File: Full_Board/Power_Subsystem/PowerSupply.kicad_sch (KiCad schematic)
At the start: 26 parts, among them IC4 LM2576HVS-5.0_NOPB, J8 KLDHCX-8-0202-A, U1 LM2576SX-3.3-NOPB

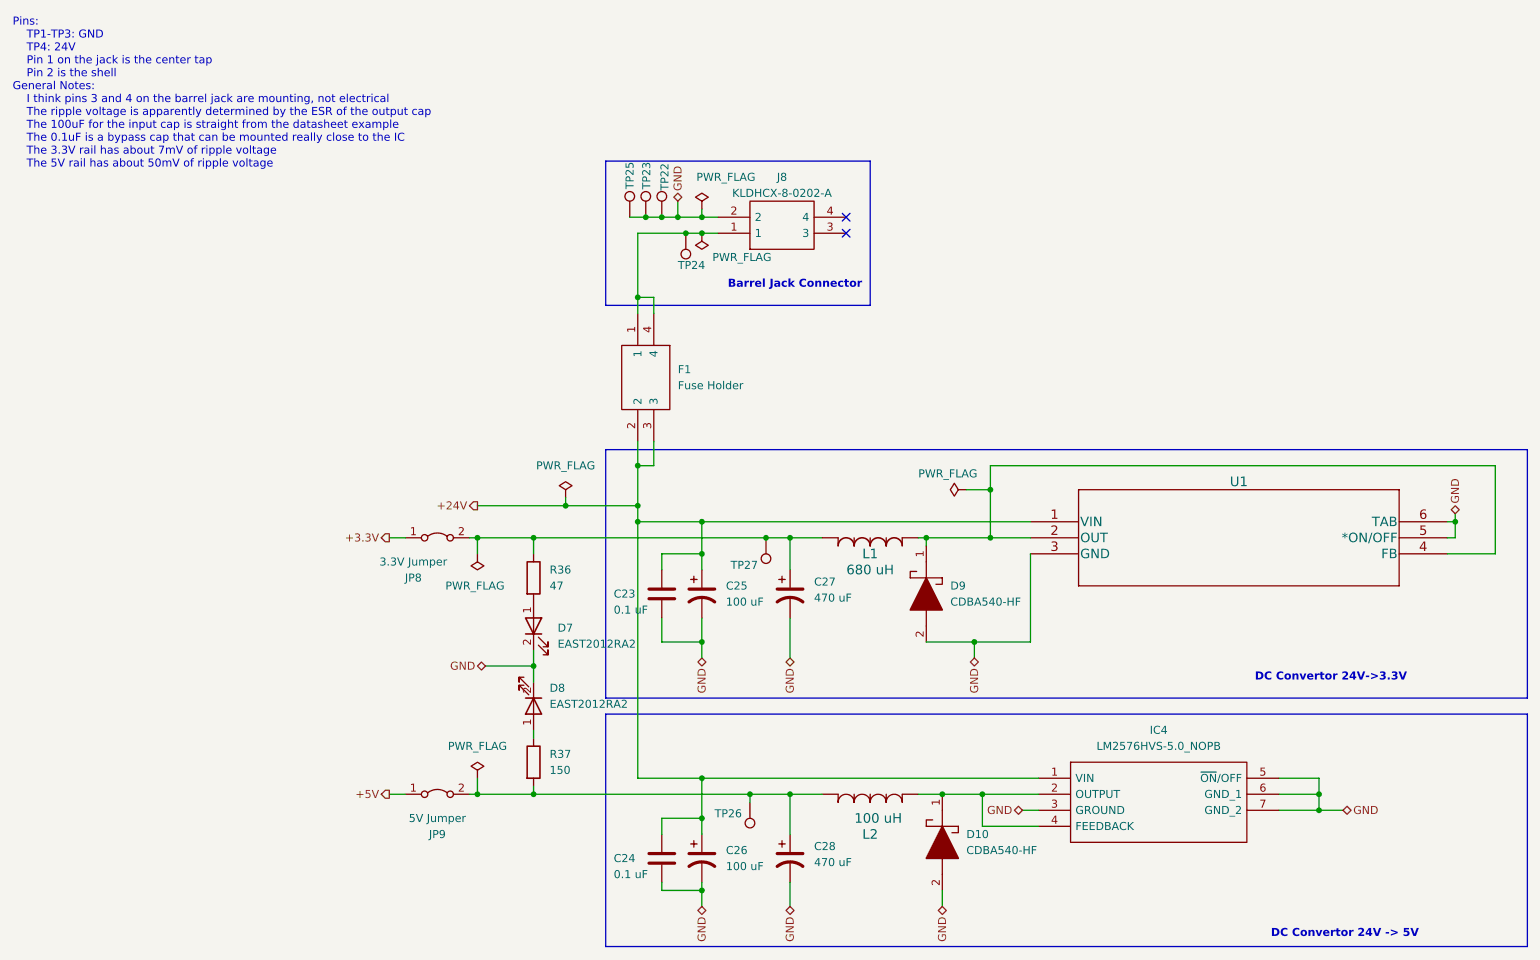
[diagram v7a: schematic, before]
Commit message: Redo pinout, finish pcb layout (no traces)
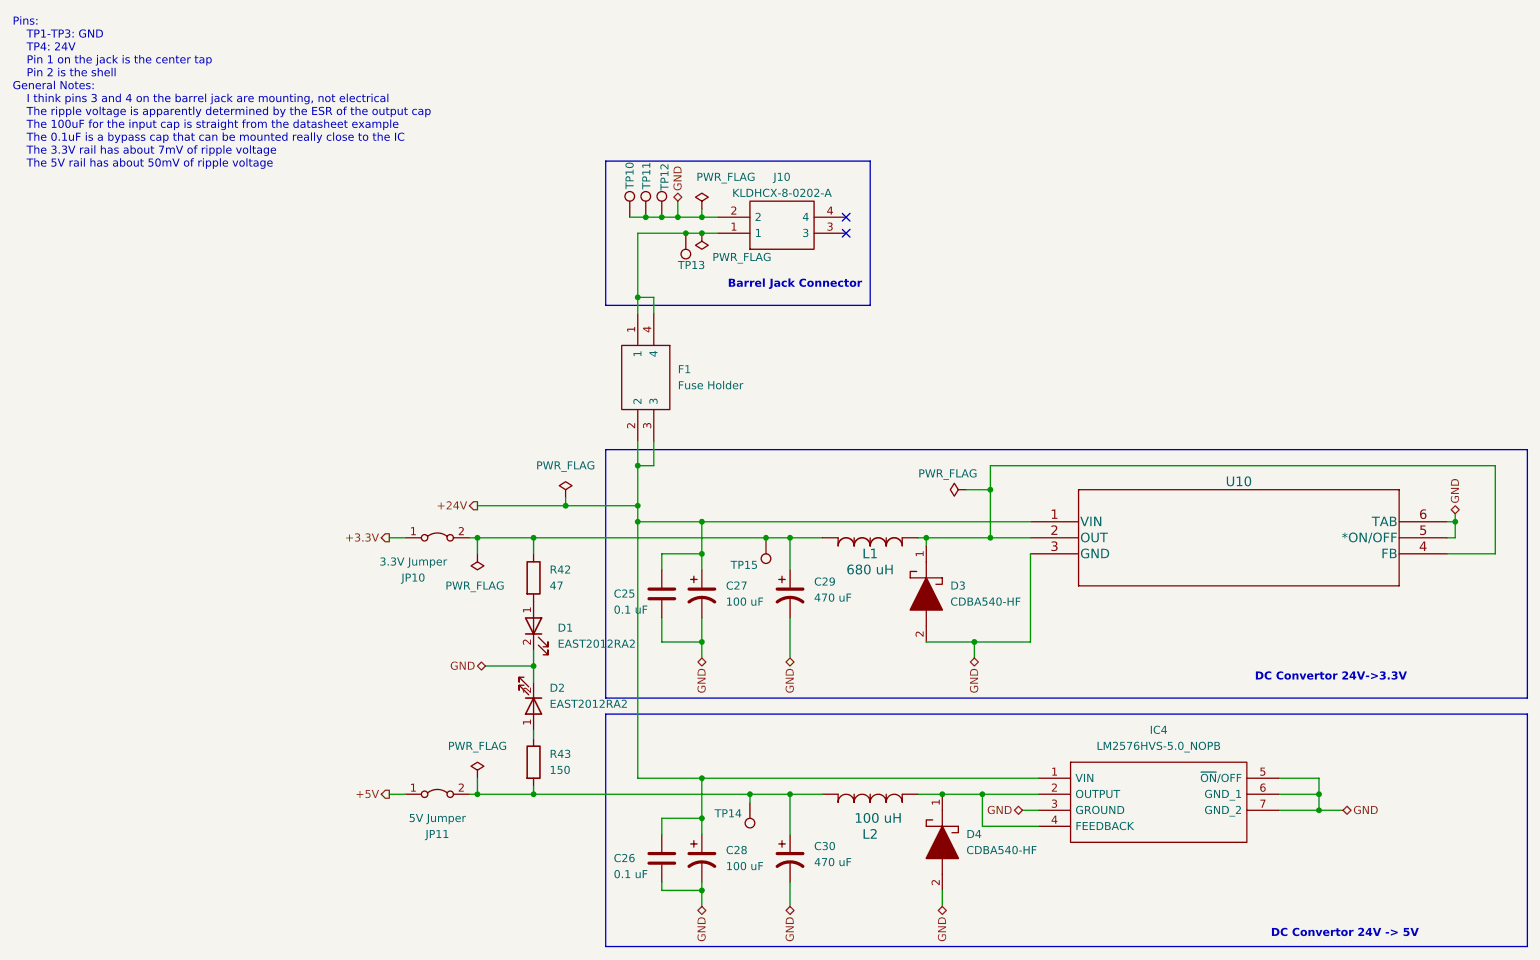
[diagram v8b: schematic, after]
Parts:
- renumbered C23 to C25, C24 to C26, C25 to C27, C26 to C28, C27 to C29, C28 to C30, D7 to D1, D8 to D2, D9 to D3, D10 to D4, J8 to J10, JP8 to JP10, JP9 to JP11, R36 to R42, R37 to R43, TP25 to TP10, TP23 to TP11, TP22 to TP12, TP24 to TP13, TP26 to TP14, TP27 to TP15, U1 to U10
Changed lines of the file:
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@@
   (symbol (lib_id "Device:C_Polarized_US") (at 140.97 146.05 0) (unit 1)
     (in_bom yes) (on_board yes) (fields_autoplaced)
-    (property "Reference" "C28" (id 0) (at 144.78 144.1449 0)
+    (property "Reference" "C30" (id 0) (at 144.78 144.1449 0)
       (effects (font (size 1.27 1.27)) (justify left))
     )
@@
   (symbol (lib_id "Device:C") (at 120.65 146.05 0) (unit 1)
     (in_bom yes) (on_board yes)
-    (property "Reference" "C24" (id 0) (at 113.03 146.05 0)
+    (property "Reference" "C26" (id 0) (at 113.03 146.05 0)
       (effects (font (size 1.27 1.27)) (justify left))
     )
@@
   (symbol (lib_id "power:PWR_FLAG") (at 127 46.99 180) (unit 1)
     (in_bom yes) (on_board yes)
-    (property "Reference" "#FLG04" (id 0) (at 127 48.895 0)
+    (property "Reference" "#FLG06" (id 0) (at 127 48.895 0)
       (effects (font (size 1.27 1.27)) hide)
     )
@@
   (symbol (lib_id "KLDHCX-8-0202-A:KLDHCX-8-0202-A") (at 129.54 46.99 0) (mirror x) (unit 1)
     (in_bom yes) (on_board yes)
-    (property "Reference" "J8" (id 0) (at 139.7 38.1 0))
+    (property "Reference" "J10" (id 0) (at 139.7 38.1 0))
     (property "Value" "KLDHCX-8-0202-A" (id 1) (at 139.7 40.64 0))
     (property "Footprint" "KLDHCX80202A" (id 2) (at 146.05 49.53 0)
@@
   (symbol (lib_id "Connector:TestPoint") (at 115.57 44.45 0) (mirror y) (unit 1)
     (in_bom yes) (on_board yes)
-    (property "Reference" "TP25" (id 0) (at 115.5876 40.0045 90)
+    (property "Reference" "TP10" (id 0) (at 115.5876 40.0045 90)
       (effects (font (size 1.27 1.27)) (justify left))
     )
@@
   (symbol (lib_id "Device:C_Polarized_US") (at 127 146.05 0) (unit 1)
     (in_bom yes) (on_board yes)
-    (property "Reference" "C26" (id 0) (at 130.81 144.78 0)
+    (property "Reference" "C28" (id 0) (at 130.81 144.78 0)
       (effects (font (size 1.27 1.27)) (justify left))
     )
@@
   (symbol (lib_id "power:PWR_FLAG") (at 105.41 88.9 0) (unit 1)
     (in_bom yes) (on_board yes) (fields_autoplaced)
-    (property "Reference" "#FLG03" (id 0) (at 105.41 86.995 0)
+    (property "Reference" "#FLG04" (id 0) (at 105.41 86.995 0)
       (effects (font (size 1.27 1.27)) hide)
     )
@@
   (symbol (lib_id "Connector:TestPoint") (at 124.46 46.99 0) (mirror x) (unit 1)
     (in_bom yes) (on_board yes)
-    (property "Reference" "TP24" (id 0) (at 123.19 52.07 0)
+    (property "Reference" "TP13" (id 0) (at 123.19 52.07 0)
       (effects (font (size 1.27 1.27)) (justify left))
     )
@@
   (symbol (lib_id "EAST2012RA2:EAST2012RA2") (at 100.33 109.22 90) (unit 1)
     (in_bom yes) (on_board yes) (fields_autoplaced)
-    (property "Reference" "D7" (id 0) (at 104.14 109.5374 90)
+    (property "Reference" "D1" (id 0) (at 104.14 109.5374 90)
       (effects (font (size 1.27 1.27)) (justify right))
     )
@@
   (symbol (lib_id "Connector:TestPoint") (at 118.11 44.45 0) (mirror y) (unit 1)
     (in_bom yes) (on_board yes)
-    (property "Reference" "TP23" (id 0) (at 118.2302 40.0244 90)
+    (property "Reference" "TP11" (id 0) (at 118.2302 40.0244 90)
       (effects (font (size 1.27 1.27)) (justify left))
     )
@@
   (symbol (lib_id "EAST2012RA2:EAST2012RA2") (at 100.33 121.92 270) (unit 1)
     (in_bom yes) (on_board yes) (fields_autoplaced)
-    (property "Reference" "D8" (id 0) (at 102.87 119.0624 90)
+    (property "Reference" "D2" (id 0) (at 102.87 119.0624 90)
       (effects (font (size 1.27 1.27)) (justify left))
     )
@@
   (symbol (lib_id "Jumper:Jumper_2_Bridged") (at 85.09 135.89 0) (unit 1)
     (in_bom yes) (on_board yes)
-    (property "Reference" "JP9" (id 0) (at 85.09 142.24 0))
+    (property "Reference" "JP11" (id 0) (at 85.09 142.24 0))
     (property "Value" "5V Jumper" (id 1) (at 85.09 139.7 0))
     (property "Footprint" "TestPoint:TestPoint_2Pads_Pitch2.54mm_Drill0.8mm" (id 2) (at 85.09 135.89 0)
@@
   (symbol (lib_id "CDBA540-HF:CDBA540-HF") (at 162.56 93.98 270) (unit 1)
     (in_bom yes) (on_board yes) (fields_autoplaced)
-    (property "Reference" "D9" (id 0) (at 166.37 102.8699 90)
+    (property "Reference" "D3" (id 0) (at 166.37 102.8699 90)
       (effects (font (size 1.27 1.27)) (justify left))
     )
@@
   (symbol (lib_id "Jumper:Jumper_2_Bridged") (at 85.09 95.25 0) (unit 1)
     (in_bom yes) (on_board yes)
-    (property "Reference" "JP8" (id 0) (at 81.28 101.6 0))
+    (property "Reference" "JP10" (id 0) (at 81.28 101.6 0))
     (property "Value" "3.3V Jumper" (id 1) (at 81.28 99.06 0))
     (property "Footprint" "TestPoint:TestPoint_2Pads_Pitch2.54mm_Drill0.8mm" (id 2) (at 85.09 95.25 0)
@@
   (symbol (lib_id "Connector:TestPoint") (at 134.62 137.16 180) (unit 1)
     (in_bom yes) (on_board yes)
-    (property "Reference" "TP26" (id 0) (at 133.35 139.7 0)
+    (property "Reference" "TP14" (id 0) (at 133.35 139.7 0)
       (effects (font (size 1.27 1.27)) (justify left top))
     )
@@
   (symbol (lib_id "Device:C") (at 120.65 104.14 0) (unit 1)
     (in_bom yes) (on_board yes)
-    (property "Reference" "C23" (id 0) (at 113.03 104.14 0)
+    (property "Reference" "C25" (id 0) (at 113.03 104.14 0)
       (effects (font (size 1.27 1.27)) (justify left))
     )
@@
   (symbol (lib_id "Device:C_Polarized_US") (at 127 104.14 0) (unit 1)
     (in_bom yes) (on_board yes)
-    (property "Reference" "C25" (id 0) (at 130.81 102.87 0)
+    (property "Reference" "C27" (id 0) (at 130.81 102.87 0)
       (effects (font (size 1.27 1.27)) (justify left))
     )
@@
   (symbol (lib_id "power:PWR_FLAG") (at 91.44 97.79 180) (unit 1)
     (in_bom yes) (on_board yes)
-    (property "Reference" "#FLG01" (id 0) (at 91.44 99.695 0)
+    (property "Reference" "#FLG02" (id 0) (at 91.44 99.695 0)
       (effects (font (size 1.27 1.27)) hide)
     )
@@
   (symbol (lib_id "Device:R") (at 100.33 101.6 0) (unit 1)
     (in_bom yes) (on_board yes) (fields_autoplaced)
-    (property "Reference" "R36" (id 0) (at 102.87 100.3299 0)
+    (property "Reference" "R42" (id 0) (at 102.87 100.3299 0)
       (effects (font (size 1.27 1.27)) (justify left))
     )
@@
   (symbol (lib_id "power:PWR_FLAG") (at 91.44 133.35 0) (unit 1)
     (in_bom yes) (on_board yes) (fields_autoplaced)
-    (property "Reference" "#FLG02" (id 0) (at 91.44 131.445 0)
+    (property "Reference" "#FLG03" (id 0) (at 91.44 131.445 0)
       (effects (font (size 1.27 1.27)) hide)
     )
@@
   (symbol (lib_id "CDBA540-HF:CDBA540-HF") (at 165.1 133.35 270) (unit 1)
     (in_bom yes) (on_board yes) (fields_autoplaced)
-    (property "Reference" "D10" (id 0) (at 168.91 142.2399 90)
+    (property "Reference" "D4" (id 0) (at 168.91 142.2399 90)
       (effects (font (size 1.27 1.27)) (justify left))
     )
@@
   (symbol (lib_id "Connector:TestPoint") (at 137.16 95.25 180) (unit 1)
     (in_bom yes) (on_board yes)
-    (property "Reference" "TP27" (id 0) (at 135.89 100.33 0)
+    (property "Reference" "TP15" (id 0) (at 135.89 100.33 0)
       (effects (font (size 1.27 1.27)) (justify left top))
     )
@@
   (symbol (lib_id "Connector:TestPoint") (at 120.65 44.45 0) (mirror y) (unit 1)
     (in_bom yes) (on_board yes)
-    (property "Reference" "TP22" (id 0) (at 121.8659 40.223 90)
+    (property "Reference" "TP12" (id 0) (at 121.8659 40.223 90)
       (effects (font (size 1.27 1.27)) (justify left top))
     )
@@
   (symbol (lib_id "LM2576SX-3.3-NOPB:LM2576SX-3.3-NOPB") (at 179.07 92.71 0) (unit 1)
     (in_bom yes) (on_board yes)
-    (property "Reference" "U1" (id 0) (at 212.09 86.36 0)
+    (property "Reference" "U10" (id 0) (at 212.09 86.36 0)
       (effects (font (size 1.524 1.524)))
     )
@@
   (symbol (lib_id "power:PWR_FLAG") (at 168.91 87.63 90) (unit 1)
     (in_bom yes) (on_board yes)
-    (property "Reference" "#FLG06" (id 0) (at 167.005 87.63 0)
+    (property "Reference" "#FLG07" (id 0) (at 167.005 87.63 0)
       (effects (font (size 1.27 1.27)) hide)
     )
@@
   (symbol (lib_id "Device:C_Polarized_US") (at 140.97 104.14 0) (unit 1)
     (in_bom yes) (on_board yes) (fields_autoplaced)
-    (property "Reference" "C27" (id 0) (at 144.78 102.2349 0)
+    (property "Reference" "C29" (id 0) (at 144.78 102.2349 0)
       (effects (font (size 1.27 1.27)) (justify left))
     )
@@
   (symbol (lib_id "Device:R") (at 100.33 130.81 0) (unit 1)
     (in_bom yes) (on_board yes) (fields_autoplaced)
-    (property "Reference" "R37" (id 0) (at 102.87 129.5399 0)
-      (effects (font (size 1.27 1.27)) (justify left))
-    )
+    (property "Reference" "R43" (id 0) (at 102.87 129.5399 0)
+      (effects (font (size 1.27 1.27)) (justify left))
+    )
